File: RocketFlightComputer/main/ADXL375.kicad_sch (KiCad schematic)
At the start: 3 parts

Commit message: Well I added a bunch of sensors, some connectors for battery, pyro channels mosfets, etc
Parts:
- added R1: 10K, ADXL375:RESPACK_4X0603, symbol Adafruit ADXL375-eagle-import:RESISTOR_4PACK
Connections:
- net ADXL375_SDO is gone; now on an unnamed net: U?.12 (ADDR/SDO)
- net +3.3V: now also R1.2 (1)
- net ADXL375_CS: no longer names the net of U?.7 (CS)
- net ADXL375_CS: now also R1.7 (2)
- net ADXL375_SCK renamed ADXL375_SCL2
- net ADXL375_SDI renamed ADXL375_SDA2
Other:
- note added: "Max current: 145 uA"
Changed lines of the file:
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@@
   (junction (at 52.705 73.66) (diameter 0) (color 0 0 0 0)
+  )
+  (junction (at 91.44 53.34) (diameter 0) (color 0 0 0 0)
   )
   (no_connect (at 57.785 63.5))
@@
     (stroke (width 0.1524) (type solid))
   )
+  (wire (pts (xy 90.17 63.5) (xy 88.265 63.5))
+    (stroke (width 0) (type default))
+  )
   (wire (pts (xy 57.785 73.66) (xy 52.705 73.66))
     (stroke (width 0.1524) (type solid))
@@
     (stroke (width 0.1524) (type solid))
   )
+  (wire (pts (xy 91.44 60.96) (xy 88.265 60.96))
+    (stroke (width 0) (type default))
+  )
   (wire (pts (xy 45.085 50.8) (xy 49.53 50.8))
     (stroke (width 0.1524) (type solid))
@@
     (stroke (width 0) (type default))
   )
+  (wire (pts (xy 91.44 52.07) (xy 91.44 53.34))
+    (stroke (width 0) (type default))
+  )
   (wire (pts (xy 57.785 76.2) (xy 52.705 76.2))
     (stroke (width 0.1524) (type solid))
@@
     (stroke (width 0.1524) (type solid))
   )
-  (wire (pts (xy 90.17 53.34) (xy 88.265 53.34))
-    (stroke (width 0) (type default))
-  )
   (wire (pts (xy 57.785 71.12) (xy 52.705 71.12))
     (stroke (width 0.1524) (type solid))
@@
     (stroke (width 0.1524) (type solid))
   )
+  (wire (pts (xy 90.17 66.04) (xy 88.265 66.04))
+    (stroke (width 0) (type default))
+  )
   (wire (pts (xy 49.53 53.34) (xy 57.785 53.34))
     (stroke (width 0) (type default))
   )
-  (text_box "Make sure to understand decoupling capacitors"
-    (at 26.035 46.99 0) (size 12.7 12.065)
+  (wire (pts (xy 88.265 53.34) (xy 91.44 53.34))
+    (stroke (width 0.1524) (type solid))
+  )
+  (wire (pts (xy 91.44 60.96) (xy 91.44 53.34))
+    (stroke (width 0) (type default))
+  )
+  (text_box "Clear BIT D6 in DATA_FORMAT register (0x31)"
+    (at 100.33 55.245 0) (size 30.48 5.08)
     (stroke (width 0) (type default))
     (fill (type none))
     (effects (font (size 1.27 1.27)) (justify left top))
   )
-  (text_box "Clear BIT D6 in DATA_FORMAT register (0x31)"
-    (at 102.87 56.515 0) (size 30.48 5.08)
+  (text_box "Adress 0x1D"
+    (at 66.04 48.26 0) (size 13.97 3.175)
     (stroke (width 0) (type default))
     (fill (type none))
     (effects (font (size 1.27 1.27)) (justify left top))
   )
-  (hierarchical_label "ADXL375_SCK" (shape input) (at 88.265 66.04 0) (fields_autoplaced)
+  (text "Max current: 145 uA\n" (at 97.79 104.14 0)
+    (effects (font (size 1.778 1.5113)) (justify left bottom))
+  )
+  (hierarchical_label "ADXL375_SCL2" (shape input) (at 90.17 66.04 0) (fields_autoplaced)
     (effects (font (size 1.27 1.27)) (justify left))
   )
-  (hierarchical_label "ADXL375_SDI" (shape input) (at 88.265 63.5 0) (fields_autoplaced)
-    (effects (font (size 1.27 1.27)) (justify left))
-  )
-  (hierarchical_label "ADXL375_CS" (shape input) (at 90.17 53.34 0) (fields_autoplaced)
-    (effects (font (size 1.27 1.27)) (justify left))
-  )
-  (hierarchical_label "ADXL375_SDO" (shape output) (at 88.265 60.96 0) (fields_autoplaced)
+  (hierarchical_label "ADXL375_SDA2" (shape input) (at 90.17 63.5 0) (fields_autoplaced)
     (effects (font (size 1.27 1.27)) (justify left))
   )
@@
     )
   )
+  (symbol (lib_id "Adafruit ADXL375-eagle-import:RESISTOR_4PACK") (at 91.44 46.99 270) (unit 2)
+    (in_bom yes) (on_board yes) (dnp no)
+    (property "Reference" "R1" (at 93.98 46.99 0)
+      (effects (font (size 1.27 1.27)))
+    )
+    (property "Value" "10K" (at 91.44 46.99 0)
+      (effects (font (size 1.016 1.016) bold))
+    )
+    (property "Footprint" "ADXL375:RESPACK_4X0603" (at 91.44 46.99 0)
+      (effects (font (size 1.27 1.27)) hide)
+    )
+    (property "Datasheet" "" (at 91.44 46.99 0)
+      (effects (font (size 1.27 1.27)) hide)
+    )
+    (pin "1")
+    (pin "8")
+    (pin "2")
+    (pin "7")
+    (pin "3")
+    (pin "6")
+    (pin "4")
+    (pin "5")
+    (instances
+      (project "Adafruit ADXL375"
+        (path "/0b998453-2602-4895-829b-1f2716a2f016"
+          (reference "R1") (unit 2)
+        )
+      )
+      (project "main"
+        (path "/27195d1d-92b2-40df-ada5-3b20841577e7/ab53b5aa-f87c-4c4c-94f1-6ed73299a675"
+          (reference "R?") (unit 2)
+        )
+      )
+    )
+  )
   (symbol (lib_id "Adafruit_BNO08x-eagle-import:CAP_CERAMIC0603_NO") (at 49.53 45.72 180) (unit 1)
     (in_bom yes) (on_board yes) (dnp no)
@@
         )
       )
+    )
+  )
+  (symbol (lib_id "power:+3.3V") (at 91.44 41.91 0) (unit 1)
+    (in_bom yes) (on_board yes) (dnp no)
+    (property "Reference" "#PWR063" (at 91.44 45.72 0)
+      (effects (font (size 1.27 1.27)) hide)
+    )
+    (property "Value" "+3.3V" (at 85.09 38.1 0)
+      (effects (font (size 1.27 1.27)) (justify left))
+    )
+    (property "Footprint" "" (at 91.44 41.91 0)
+      (effects (font (size 1.27 1.27)) hide)
+    )
+    (property "Datasheet" "" (at 91.44 41.91 0)
+      (effects (font (size 1.27 1.27)) hide)
+    )
+    (pin "1")
+    (instances
+      (project "main"
+        (path "/27195d1d-92b2-40df-ada5-3b20841577e7"
+          (reference "#PWR063") (unit 1)
+        )
+        (path "/27195d1d-92b2-40df-ada5-3b20841577e7/cea4c1d7-5261-445d-b36e-014b1552505a"
+          (reference "#PWR073") (unit 1)
+        )
+        (path "/27195d1d-92b2-40df-ada5-3b20841577e7/ab53b5aa-f87c-4c4c-94f1-6ed73299a675"
+          (reference "#PWR098") (unit 1)
+        )
+      )

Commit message: Addition of telemetry is pcb schematic
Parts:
- gave numbers to parts that had none: 3
- renumbered R1 to R?

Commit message: The design is getting more mature, still did not choose if doing 4 layers or 2 layers pcb, will try to add 5v for a on board camera and trace routes for reserved pins in case of usage on another vehicle
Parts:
- removed R?: 10K, ADXL375:RESPACK_4X0603, symbol Adafruit ADXL375-eagle-import:RESISTOR_4PACK
- added R14: 10k, Resistor_SMD:R_0603_1608Metric_Pad0.98x0.95mm_HandSolder, symbol Device:R
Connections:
- net +3.3V: now also R14.1
- net at U2.12 (ADDR/SDO), U2.7 (CS): now also R14.2
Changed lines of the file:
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@@
+		)
+	)
+	(text_box "I2C mode"
+		(exclude_from_sim no)
+		(at 66.04 35.56 0)
+		(size 12.7 5.08)
+		(stroke
+			(width 0)
+			(type default)
+		)
+		(fill
+			(type none)
+		)
+		(effects
+			(font
+				(size 1.27 1.27)
+			)
+			(justify left top)
 		)
 	)
@@
 	)
 	(symbol
-		(lib_id "Adafruit ADXL375-eagle-import:RESISTOR_4PACK")
-		(at 91.44 46.99 270)
-		(unit 2)
-		(exclude_from_sim no)
-		(in_bom yes)
-		(on_board yes)
-		(dnp no)
-		(property "Reference" "R?"
-			(at 93.98 46.99 0)
-			(effects
-				(font
-					(size 1.27 1.27)
-				)
-			)
-		)
-		(property "Value" "10K"
-			(at 91.44 46.99 0)
-			(effects
-				(font
-					(size 1.016 1.016)
-					(bold yes)
-				)
-			)
-		)
-		(property "Footprint" "ADXL375:RESPACK_4X0603"
-			(at 91.44 46.99 0)
-			(effects
-				(font
-					(size 1.27 1.27)
-				)
-				(hide yes)
-			)
-		)
-		(property "Datasheet" ""
-			(at 91.44 46.99 0)
-			(effects
-				(font
-					(size 1.27 1.27)
-				)
-				(hide yes)
-			)
-		)
-		(property "Description" ""
-			(at 91.44 46.99 0)
-			(effects
-				(font
-					(size 1.27 1.27)
-				)
-				(hide yes)
-			)
-		)
-		(pin "1"
-		)
-		(pin "8"
-		)
-		(pin "2"
-		)
-		(pin "7"
-		)
-		(pin "3"
-		)
-		(pin "6"
-		)
-		(pin "4"
-		)
-		(pin "5"
-		)
-		(instances
-			(project "Adafruit ADXL375"
-				(path "/0b998453-2602-4895-829b-1f2716a2f016"
-					(reference "R?")
-					(unit 2)
-				)
-			)
-			(project "main"
-				(path "/27195d1d-92b2-40df-ada5-3b20841577e7/ab53b5aa-f87c-4c4c-94f1-6ed73299a675"
-					(reference "R11")
-					(unit 2)
-				)
-			)
-		)
-	)
-	(symbol
 		(lib_id "Adafruit_BNO08x-eagle-import:CAP_CERAMIC0603_NO")
 		(at 49.53 45.72 180)
@@
 	(symbol
 		(lib_id "power:+3.3V")
-		(at 91.44 41.91 0)
+		(at 91.44 44.45 0)
 		(unit 1)
 		(exclude_from_sim no)
@@
 		(dnp no)
 		(property "Reference" "#PWR094"
-			(at 91.44 45.72 0)
+			(at 91.44 48.26 0)
 			(effects
 				(font
@@
 		)
 		(property "Value" "+3.3V"
-			(at 85.09 38.1 0)
+			(at 90.424 40.386 0)
 			(effects
 				(font
@@
 		)
 		(property "Footprint" ""
-			(at 91.44 41.91 0)
-			(effects
-				(font
-					(size 1.27 1.27)
-				)
-				(hide yes)
-			)
-		)
-		(property "Datasheet" ""
-			(at 91.44 41.91 0)
-			(effects
-				(font
-					(size 1.27 1.27)
-				)
-				(hide yes)
-			)
-		)
-		(property "Description" ""
-			(at 91.44 41.91 0)
+			(at 91.44 44.45 0)
+			(effects
+				(font
+					(size 1.27 1.27)
+				)
+				(hide yes)
+			)
+		)
+		(property "Datasheet" ""
+			(at 91.44 44.45 0)
+			(effects
+				(font
+					(size 1.27 1.27)
+				)
+				(hide yes)
+			)
+		)
+		(property "Description" ""
+			(at 91.44 44.45 0)
 			(effects
 				(font
@@
 		(on_board yes)
 		(dnp no)
-		(property "Reference" "#PWR090"
+		(property "Reference" "#PWR0150"
 			(at 48.895 53.34 0)
 			(effects
@@
 			(project "main"
 				(path "/27195d1d-92b2-40df-ada5-3b20841577e7/ab53b5aa-f87c-4c4c-94f1-6ed73299a675"
-					(reference "#PWR090")
+					(reference "#PWR0150")
 					(unit 1)
 				)
@@
 	)
 	(symbol
+		(lib_id "Device:R")
+		(at 91.44 48.26 0)
+		(unit 1)
+		(exclude_from_sim no)
+		(in_bom yes)
+		(on_board yes)
+		(dnp no)
+		(property "Reference" "R14"
+			(at 93.98 48.26 90)
+			(effects
+				(font
+					(size 1.27 1.27)
+				)
+			)
+		)
+		(property "Value" "10k"
+			(at 91.44 45.974 90)
+			(effects
+				(font
+					(size 1.27 1.27)
+				)
+				(justify right)
+			)
+		)
+		(property "Footprint" "Resistor_SMD:R_0603_1608Metric_Pad0.98x0.95mm_HandSolder"
+			(at 89.662 48.26 90)
+			(effects
+				(font
+					(size 1.27 1.27)
+				)
+				(hide yes)
+			)
+		)
+		(property "Datasheet" "~"
+			(at 91.44 48.26 0)
+			(effects
+				(font
+					(size 1.27 1.27)
+				)
+				(hide yes)
+			)
+		)
+		(property "Description" ""
+			(at 91.44 48.26 0)
+			(effects
+				(font
+					(size 1.27 1.27)
+				)
+				(hide yes)
+			)
+		)
+		(pin "1"
+		)
+		(pin "2"
+		)
+		(instances
+			(project "main"
+				(path "/27195d1d-92b2-40df-ada5-3b20841577e7/ab53b5aa-f87c-4c4c-94f1-6ed73299a675"
+					(reference "R14")
+					(unit 1)
+				)
+			)
+		)
+	)
+	(symbol
 		(lib_id "power:GNDREF")
 		(at 49.53 60.96 0)
@@
 		(on_board yes)
 		(dnp no)
-		(property "Reference" "#PWR089"
+		(property "Reference" "#PWR0151"
 			(at 48.895 50.8 0)
 			(effects
@@
 			(project "main"
 				(path "/27195d1d-92b2-40df-ada5-3b20841577e7/ab53b5aa-f87c-4c4c-94f1-6ed73299a675"
-					(reference "#PWR089")
-					(unit 1)
-				)
+					(reference "#PWR0151")
+					(unit 1)
+				)

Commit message: Layout of PCB mostly done
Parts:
- ADXL375: renamed from U2; value ADXL375 -> ACC; footprint ADXL375:LGA14 -> footprint:ADXL375BCCZRL
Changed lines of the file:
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@@
 		(on_board yes)
 		(dnp no)
-		(property "Reference" "U2"
+		(property "Reference" "ADXL375"
 			(at 60.325 37.338 0)
 			(effects
@@
 				)
 				(justify left bottom)
+				(hide yes)
 			)
 		)
-		(property "Value" "ADXL375"
+		(property "Value" "ACC"
 			(at 60.325 88.9 0)
 			(effects
@@
 			)
 		)
-		(property "Footprint" "ADXL375:LGA14"
+		(property "Footprint" "footprint:ADXL375BCCZRL"
 			(at 73.025 63.5 0)
 			(effects
@@
 			(project "main"
 				(path "/27195d1d-92b2-40df-ada5-3b20841577e7/ab53b5aa-f87c-4c4c-94f1-6ed73299a675"
-					(reference "U2")
+					(reference "ADXL375")
 					(unit 1)
 				)

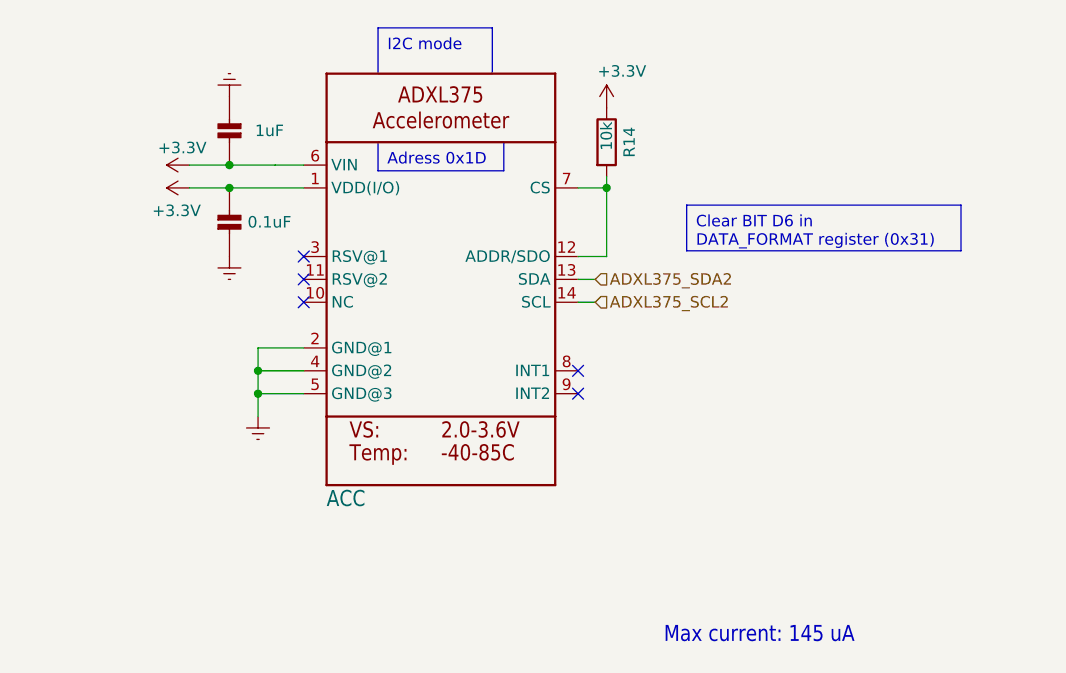
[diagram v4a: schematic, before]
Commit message: First pass of verification and validation of pcb design
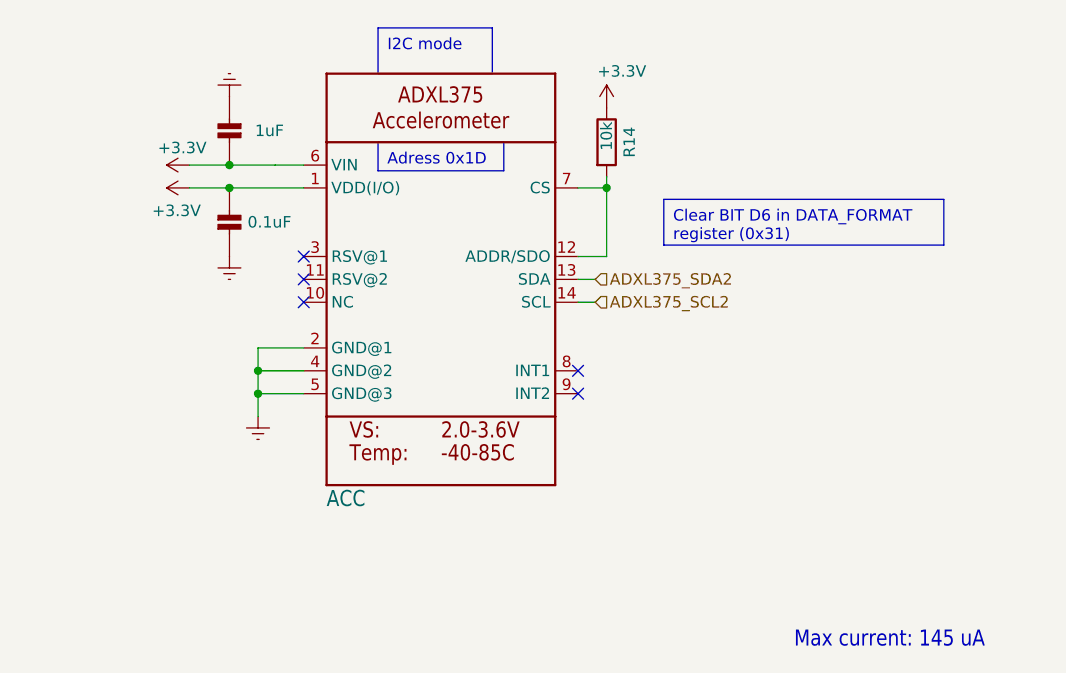
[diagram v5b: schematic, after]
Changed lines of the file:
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@@
 	(text_box "Clear BIT D6 in DATA_FORMAT register (0x31)"
 		(exclude_from_sim no)
-		(at 100.33 55.245 0)
-		(size 30.48 5.08)
+		(at 97.79 54.61 0)
+		(size 31.115 5.08)
 		(stroke
 			(width 0)
@@
 	(text "Max current: 145 uA\n"
 		(exclude_from_sim no)
-		(at 97.79 104.14 0)
+		(at 112.268 104.648 0)
 		(effects
 			(font

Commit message: Addition of all components in BOM, metal mounting plates, need to check psram if its ok for signals to pass under, all components need a double check
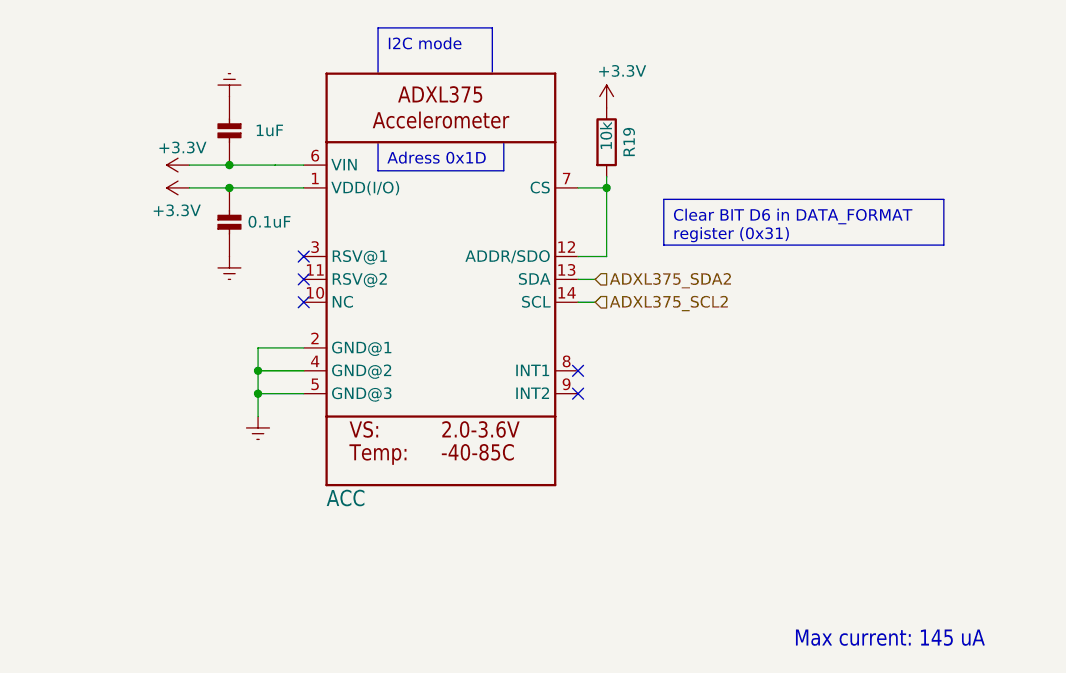
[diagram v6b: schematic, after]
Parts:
- ADXL1: renamed from ADXL375; LCSC (none) -> C579466; Mouser Part Number (none) -> 584-ADXL375BCCZ
- C36: renamed from C35; LCSC (none) -> C1592
- C37: renamed from C36; LCSC (none) -> C48579250
- R19: renamed from R14; LCSC (none) -> C25804
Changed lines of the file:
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@@
 		(on_board yes)
 		(dnp no)
-		(property "Reference" "C36"
+		(property "Reference" "C37"
 			(at 47.24 57.17 0)
 			(effects
@@
 			)
 		)
+		(property "LCSC" "C48579250"
+			(at 49.53 58.42 0)
+			(effects
+				(font
+					(size 1.27 1.27)
+				)
+				(hide yes)
+			)
+		)
 		(pin "1"
 		)
@@
 			(project "main"
 				(path "/27195d1d-92b2-40df-ada5-3b20841577e7/ab53b5aa-f87c-4c4c-94f1-6ed73299a675"
-					(reference "C36")
+					(reference "C37")
 					(unit 1)
 				)
@@
 		(dnp no)
 		(fields_autoplaced yes)
-		(property "Reference" "#PWR093"
+		(property "Reference" "#PWR0100"
 			(at 52.705 85.09 0)
 			(effects
@@
 			(project "main"
 				(path "/27195d1d-92b2-40df-ada5-3b20841577e7/ab53b5aa-f87c-4c4c-94f1-6ed73299a675"
-					(reference "#PWR093")
+					(reference "#PWR0100")
 					(unit 1)
 				)
@@
 		(on_board yes)
 		(dnp no)
-		(property "Reference" "ADXL375"
+		(property "Reference" "ADXL1"
 			(at 60.325 37.338 0)
 			(effects
@@
 			)
 		)
+		(property "LCSC" "C579466 "
+			(at 73.025 63.5 0)
+			(effects
+				(font
+					(size 1.27 1.27)
+				)
+				(hide yes)
+			)
+		)
+		(property "Mouser Part Number" "584-ADXL375BCCZ"
+			(at 73.025 63.5 0)
+			(effects
+				(font
+					(size 1.27 1.27)
+				)
+				(hide yes)
+			)
+		)
 		(pin "1"
 		)
@@
 			(project "main"
 				(path "/27195d1d-92b2-40df-ada5-3b20841577e7/ab53b5aa-f87c-4c4c-94f1-6ed73299a675"
-					(reference "ADXL375")
+					(reference "ADXL1")
 					(unit 1)
 				)
@@
 		(on_board yes)
 		(dnp no)
-		(property "Reference" "C35"
+		(property "Reference" "C36"
 			(at 51.82 46.97 0)
 			(effects
@@
 			)
 		)
+		(property "LCSC" "C1592 "
+			(at 49.53 45.72 0)
+			(effects
+				(font
+					(size 1.27 1.27)
+				)
+				(hide yes)
+			)
+		)
 		(pin "1"
 		)
@@
 			(project "main"
 				(path "/27195d1d-92b2-40df-ada5-3b20841577e7/ab53b5aa-f87c-4c4c-94f1-6ed73299a675"
-					(reference "C35")
+					(reference "C36")
 					(unit 1)
 				)
@@
 		(on_board yes)
 		(dnp no)
-		(property "Reference" "#PWR094"
+		(property "Reference" "#PWR0101"
 			(at 91.44 48.26 0)
 			(effects
@@
 			(project "main"
 				(path "/27195d1d-92b2-40df-ada5-3b20841577e7/ab53b5aa-f87c-4c4c-94f1-6ed73299a675"
-					(reference "#PWR094")
+					(reference "#PWR0101")
 					(unit 1)
 				)
@@
 		(on_board yes)
 		(dnp no)
-		(property "Reference" "#PWR0150"
+		(property "Reference" "#PWR097"
 			(at 48.895 53.34 0)
 			(effects
@@
 			(project "main"
 				(path "/27195d1d-92b2-40df-ada5-3b20841577e7/ab53b5aa-f87c-4c4c-94f1-6ed73299a675"
-					(reference "#PWR0150")
+					(reference "#PWR097")
 					(unit 1)
 				)
@@
 		(dnp no)
 		(fields_autoplaced yes)
-		(property "Reference" "#PWR091"
+		(property "Reference" "#PWR098"
 			(at 49.53 36.83 0)
 			(effects
@@
 			(project "main"
 				(path "/27195d1d-92b2-40df-ada5-3b20841577e7/ab53b5aa-f87c-4c4c-94f1-6ed73299a675"
-					(reference "#PWR091")
+					(reference "#PWR098")
 					(unit 1)
 				)
@@
 		(on_board yes)
 		(dnp no)
-		(property "Reference" "R14"
+		(property "Reference" "R19"
 			(at 93.98 48.26 90)
 			(effects
@@
 			)
 		)
+		(property "LCSC" "C25804 "
+			(at 91.44 48.26 0)
+			(effects
+				(font
+					(size 1.27 1.27)
+				)
+				(hide yes)
+			)
+		)
 		(pin "1"
 		)
@@
 			(project "main"
 				(path "/27195d1d-92b2-40df-ada5-3b20841577e7/ab53b5aa-f87c-4c4c-94f1-6ed73299a675"
-					(reference "R14")
+					(reference "R19")
 					(unit 1)
 				)
@@
 		(dnp no)
 		(fields_autoplaced yes)
-		(property "Reference" "#PWR092"
+		(property "Reference" "#PWR099"
 			(at 49.53 67.31 0)
 			(effects
@@
 			(project "main"
 				(path "/27195d1d-92b2-40df-ada5-3b20841577e7/ab53b5aa-f87c-4c4c-94f1-6ed73299a675"
-					(reference "#PWR092")
+					(reference "#PWR099")
 					(unit 1)
 				)
@@
 		(on_board yes)
 		(dnp no)
-		(property "Reference" "#PWR0151"
+		(property "Reference" "#PWR096"
 			(at 48.895 50.8 0)
 			(effects
@@
 			(project "main"
 				(path "/27195d1d-92b2-40df-ada5-3b20841577e7/ab53b5aa-f87c-4c4c-94f1-6ed73299a675"
-					(reference "#PWR0151")
-					(unit 1)
-				)
+					(reference "#PWR096")
+					(unit 1)
+				)

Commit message: Change of winbond flash to other one supported by teensy bootloader since winbond is out of stock
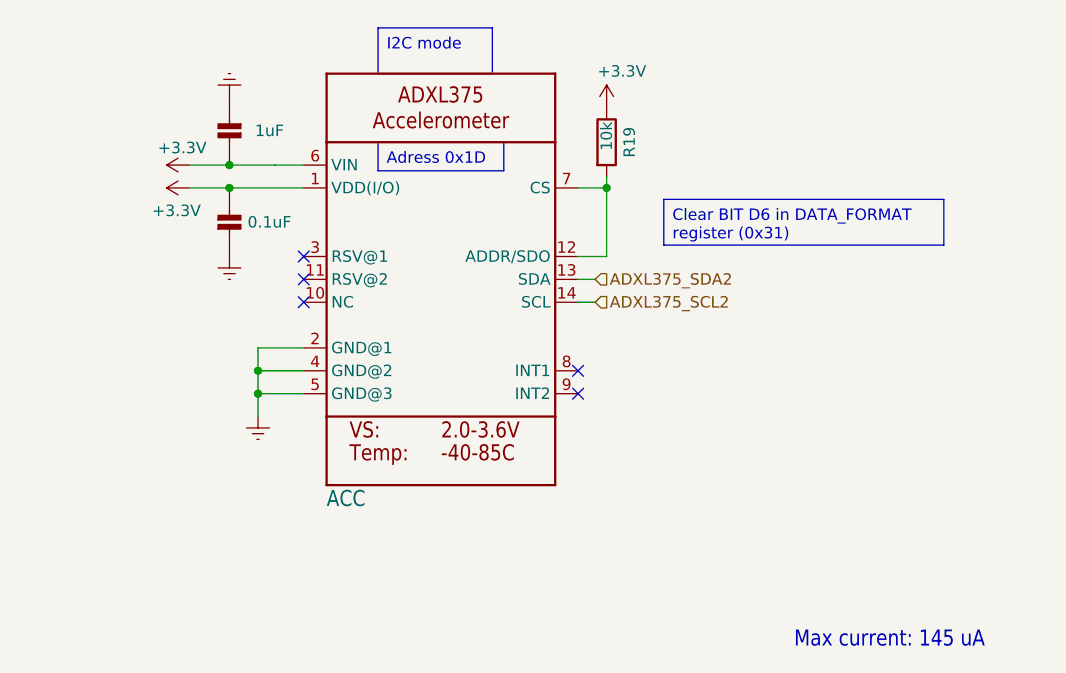
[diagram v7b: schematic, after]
